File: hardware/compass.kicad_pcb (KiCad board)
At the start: 2 copper layers, 25 x 20 mm, 19 parts, among them P1 CON-SENSOR2, P2 DEBUG, P3 BOOT, U1 XMC1XXX24, U2 MMC5883MA, U3 DRILL, U4 DRILL, U5 DRILL, U6 DRILL

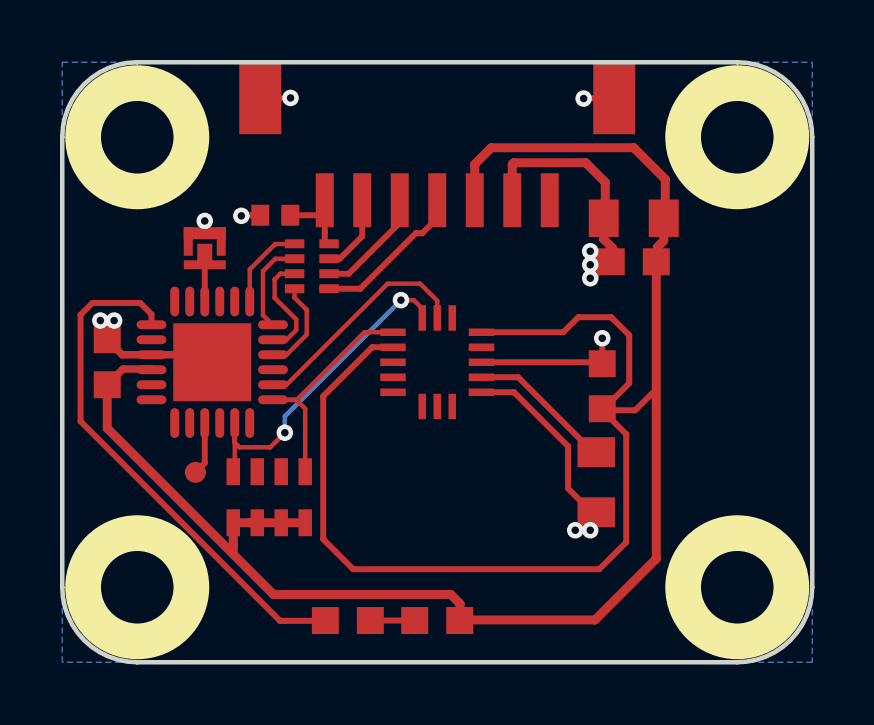
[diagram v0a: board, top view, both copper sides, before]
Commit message: added silkscreen
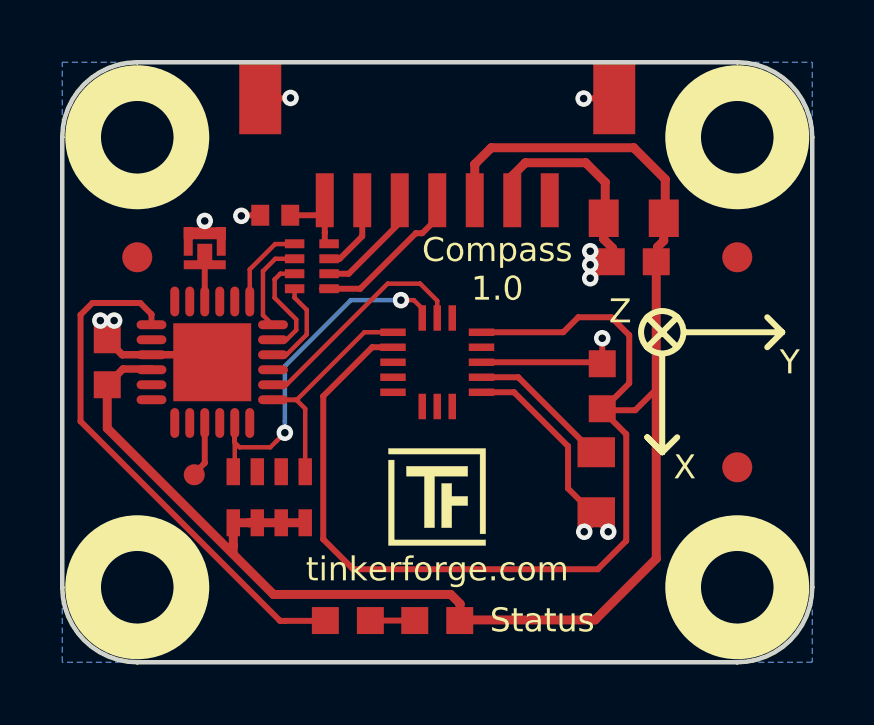
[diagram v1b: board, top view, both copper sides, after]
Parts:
- added Fiducial_Mark: VAL**, kicad-libraries:Fiducial_Mark, F.Cu at (160.0, 94.0)
- added Fiducial_Mark: VAL**, kicad-libraries:Fiducial_Mark, F.Cu at (180.0, 94.0)
- added Fiducial_Mark: VAL**, kicad-libraries:Fiducial_Mark, F.Cu at (180.0, 101.0)
- added G***: LOGO, kicad-libraries:Logo_CoMCU, B.Cu at (176.5, 97.0)
- added G***: LOGO, kicad-libraries:Logo_31x31, F.Cu at (170.0, 102.0)
- added VAL: WEEE_7mm, kicad-libraries:WEEE_7mm, B.Cu at (170.0, 97.0)
- added VAL: CE_5mm, kicad-libraries:CE_5mm, B.Cu at (163.5, 97.0)
- moved P2 0.09 mm to (161.9, 101.2)
- turned C6 to 270 degrees
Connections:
- C6 pad 1: GND -> Net-(C6-Pad1)
- U2 pad 10: GND -> Net-(C6-Pad1)
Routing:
- net GND: track 40.8 -> 35.5 mm
- net Net-(C6-Pad1): track 0.00 -> 4.86 mm
- net SDA: track 11.5 -> 12.5 mm
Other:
- net class Default: clearance 0.2 -> 0.15
- rule trace_clearance: 0.2 -> 0.15
- board text added: "Compass 1.0"
- board text added: "Status"
- board text added: "X"
- board text added: "Y"
- board text added: "Z"
- board text added: "tinkerforge.com"

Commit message: changed footprint of MMC to LGA16
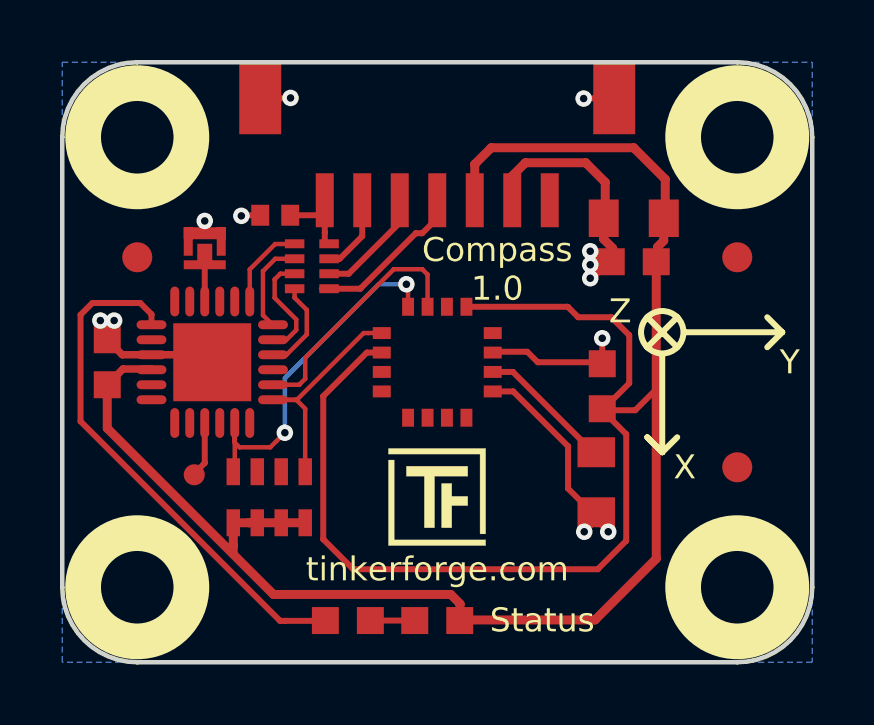
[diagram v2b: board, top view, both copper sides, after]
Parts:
- U2: footprint kicad-libraries:LGA-16-3x3 -> tinkerforge:LGA-16
- turned U2 to 270 degrees
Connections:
- P1 pad 1: (no net) -> Net-(P1-Pad1)
- RP2 pad 6: (no net) -> Net-(RP2-Pad6)
- RP2 pad 7: (no net) -> Net-(RP2-Pad7)
- U1 pad 11: (no net) -> Net-(U1-Pad11)
- U1 pad 12: (no net) -> Net-(U1-Pad12)
- U1 pad 13: (no net) -> Net-(U1-Pad13)
- U1 pad 14: (no net) -> Net-(U1-Pad14)
- U1 pad 16: (no net) -> Net-(U1-Pad16)
- U1 pad 18: (no net) -> Net-(U1-Pad18)
- U1 pad 2: (no net) -> Net-(U1-Pad2)
- U1 pad 21: (no net) -> Net-(U1-Pad21)
- U1 pad 3: (no net) -> Net-(U1-Pad3)
- U1 pad 5: (no net) -> Net-(U1-Pad5)
- U1 pad 6: (no net) -> Net-(U1-Pad6)
- U1 pad 8: (no net) -> Net-(U1-Pad8)
- U2 pad 12: (no net) -> Net-(U2-Pad12)
- U2 pad 14: (no net) -> Net-(U2-Pad14)
- U2 pad 3: (no net) -> Net-(U2-Pad3)
- U2 pad 4: (no net) -> Net-(U2-Pad4)
- U2 pad 5: (no net) -> Net-(U2-Pad5)
- U2 pad 6: (no net) -> Net-(U2-Pad6)
- U2 pad 7: (no net) -> Net-(U2-Pad7)
- U2 pad 8: (no net) -> Net-(U2-Pad8)
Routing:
- net INTERRUPT: track 7.69 -> 8.31 mm
- net GND: track 35.5 -> 34.9 mm

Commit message: updated footprint to LGA-16-3x3_Compass, moved some caps for better screw clearance
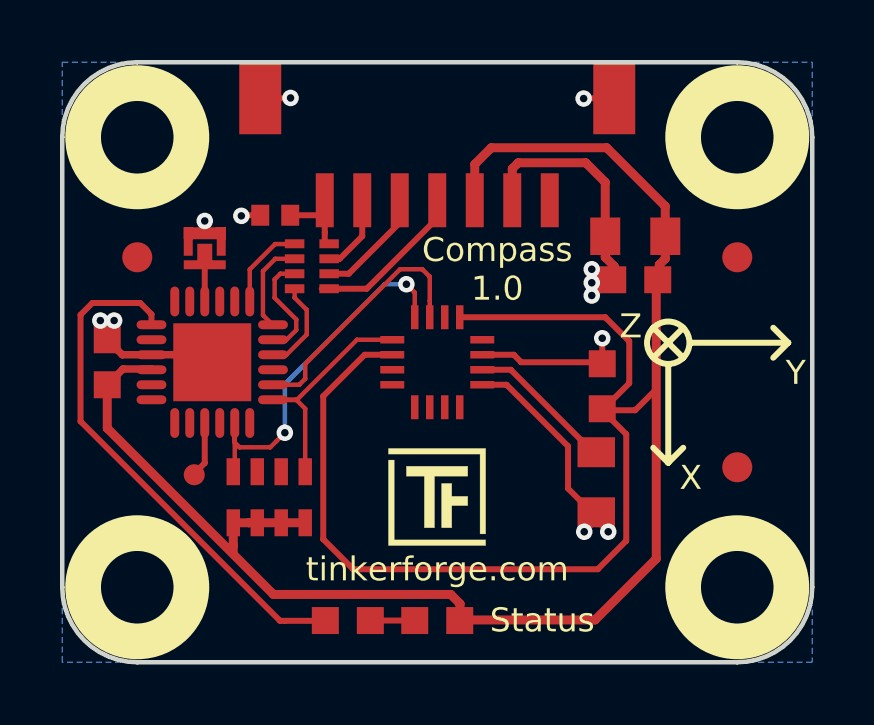
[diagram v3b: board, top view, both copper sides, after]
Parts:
- U2: footprint tinkerforge:LGA-16 -> kicad-libraries:LGA16-3x3_Compass
- moved C4 0.60 mm to (176.6, 93.3)
- moved C5 0.60 mm to (176.6, 94.8)
- turned U2 to 90 degrees
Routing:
- net GND: track 34.9 -> 35.8 mm
- net VCC: track 83.8 -> 82.9 mm
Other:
- rule pad_to_mask_clearance: 0.051 -> 0

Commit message: changed co-processor to xmc1300
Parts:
- U1: value XMC1XXX24 -> XMC1300
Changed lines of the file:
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@@
       (layerselection 0x010fc_ffffffff)
       (usegerberextensions true)
-      (usegerberattributes false)
+      (usegerberattributes true)
       (usegerberadvancedattributes false)
       (creategerberjobfile false)
@@
       (effects (font (size 0.3 0.3) (thickness 0.075)))
     )
-    (fp_text value XMC1XXX24 (at 0 0.8 270) (layer F.Fab)
+    (fp_text value XMC1300 (at 0 0.8 270) (layer F.Fab)
       (effects (font (size 0.3 0.3) (thickness 0.075)))
     )
